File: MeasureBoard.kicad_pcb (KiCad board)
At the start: 2 copper layers, 60 x 80 mm, 129 parts, among them J1 Conn_01x06, J10 Conn_02x05_Odd_Even, J11 Conn_01x04, J12 Conn_01x06, J13 GS3, J14 USB_OTG, J15 Conn_01x02, J17 Conn_01x02, J18 Conn_01x03, J19 Conn_01x03, J2 Conn_01x04, J20 Conn_01x03, J21 Conn_01x03, J22 Conn_01x03, J23 Conn_01x03, J24 Conn_02x05_Odd_Even, J25 TEST_1P, J26 TEST_1P, J27 TEST_1P, J28 TEST_1P, J3 GS3, J4 GS2, J5 Conn_01x04, J6 Conn_01x03, J7 Conn_01x04, J8 BARREL_JACK, J9 CONN_01X02, SW1 DIP_SW_2P, SW2 SKRPACE010, SW3 SKRPACE010, SW4 SKRPACE010, U1 L7805, U2 AP1117-33, U3 STM32F103CBTx, U4 NC7SZ08, U5 SP3481CN, U6 NC7WZ241, U7 LTC2875-S8, U8 AM26LV32, Y1 Crystal

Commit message: gndのパスを修正
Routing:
- net GND: track 673.7 -> 663.9 mm, vias 119 -> 115
- net +5V: track 183.6 -> 188.9 mm
- net (no net): track 0.00 -> 1.64 mm, vias 0 -> 2
- net /CAN/CAN_H: track 13.1 -> 11.6 mm
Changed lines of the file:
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@@
-(kicad_pcb (version 4) (host pcbnew 4.0.7)
+(kicad_pcb (version 4) (host pcbnew 4.0.6)
   (general
     (links 311)
@@
     (thickness 1.6)
     (drawings 149)
-    (tracks 1607)
+    (tracks 1605)
     (zones 0)
     (modules 129)
@@
   (gr_line (start 54 150) (end 106 150) (layer Edge.Cuts) (width 0.15))
   (gr_line (start 50 74) (end 50 146) (layer Edge.Cuts) (width 0.15))
+  (segment (start 92 94.5) (end 90.5 94.5) (width 0.25) (layer F.Cu) (net 0))
+  (via (at 90.5 94.5) (size 0.6) (drill 0.4) (layers F.Cu B.Cu) (net 0))
+  (segment (start 92.1 94.6) (end 92 94.5) (width 0.25) (layer B.Cu) (net 0))
+  (via (at 92 94.5) (size 0.6) (drill 0.4) (layers F.Cu B.Cu) (net 0))
+  (segment (start 96 105.7) (end 95.35 105.7) (width 0.25) (layer F.Cu) (net 1))
+  (segment (start 95.35 105.7) (end 93.599999 107.450001) (width 0.25) (layer F.Cu) (net 1))
+  (segment (start 93.599999 107.450001) (end 93.599999 109.700001) (width 0.25) (layer F.Cu) (net 1))
+  (segment (start 93.599999 109.700001) (end 93.3 110) (width 0.25) (layer F.Cu) (net 1))
+  (segment (start 101 114.1) (end 99.93 114.1) (width 0.25) (layer F.Cu) (net 1))
+  (segment (start 99.93 114.1) (end 98.5 112.67) (width 0.25) (layer F.Cu) (net 1))
   (segment (start 93.6 113.3) (end 93.6 114.7) (width 0.25) (layer F.Cu) (net 1))
   (segment (start 93.6 114.7) (end 93.6 114.89) (width 0.25) (layer F.Cu) (net 1))
@@
   (segment (start 78.7 134) (end 78.9 133.8) (width 0.25) (layer B.Cu) (net 1))
   (via (at 78.9 133.8) (size 0.6) (drill 0.4) (layers F.Cu B.Cu) (net 1))
-  (segment (start 105.4 117.7) (end 103.7 117.7) (width 0.25) (layer F.Cu) (net 1))
-  (segment (start 103.7 117.7) (end 103.3 118.1) (width 0.25) (layer F.Cu) (net 1))
-  (via (at 103.3 118.1) (size 0.6) (drill 0.4) (layers F.Cu B.Cu) (net 1))
   (segment (start 101 114.1) (end 99.6 114.1) (width 0.25) (layer B.Cu) (net 1))
   (segment (start 99.6 114.1) (end 99 114.7) (width 0.25) (layer B.Cu) (net 1))
@@
   (via (at 93.8 89.8) (size 0.8) (drill 0.6) (layers F.Cu B.Cu) (net 1))
   (via (at 90.6 89.8) (size 0.8) (drill 0.6) (layers F.Cu B.Cu) (net 1))
-  (via (at 93.8 100) (size 0.8) (drill 0.6) (layers F.Cu B.Cu) (net 1))
   (segment (start 90.4 98.6) (end 90.4 100.6) (width 0.25) (layer B.Cu) (net 1))
   (via (at 90.4 100.6) (size 0.8) (drill 0.6) (layers F.Cu B.Cu) (net 1))
@@
   (segment (start 90.6 89.8) (end 93.8 89.8) (width 0.25) (layer F.Cu) (net 1))
   (segment (start 89.1 89.8) (end 90.6 89.8) (width 0.25) (layer B.Cu) (net 1))
-  (segment (start 92 94.5) (end 90.5 94.5) (width 0.25) (layer F.Cu) (net 1))
-  (via (at 90.5 94.5) (size 0.6) (drill 0.4) (layers F.Cu B.Cu) (net 1))
-  (segment (start 92.1 94.6) (end 92 94.5) (width 0.25) (layer B.Cu) (net 1))
-  (via (at 92 94.5) (size 0.6) (drill 0.4) (layers F.Cu B.Cu) (net 1))
   (segment (start 93.8 91.4) (end 93.8 93) (width 0.25) (layer B.Cu) (net 1))
   (segment (start 86.6 91.4) (end 93.8 91.4) (width 0.25) (layer F.Cu) (net 1))
@@
   (via (at 88.5 110.8) (size 0.6) (drill 0.4) (layers F.Cu B.Cu) (net 1))
   (via (at 93.3 110) (size 0.6) (drill 0.4) (layers F.Cu B.Cu) (net 1))
-  (segment (start 93.1 110.2) (end 93.3 110) (width 0.25) (layer F.Cu) (net 1))
   (segment (start 81.7 131.6) (end 81.7 133.5) (width 0.25) (layer F.Cu) (net 1))
   (via (at 81.6 133.6) (size 0.6) (drill 0.4) (layers F.Cu B.Cu) (net 1))
@@
   (segment (start 79.324264 134.4) (end 81.7 132.024264) (width 0.25) (layer F.Cu) (net 1))
   (segment (start 81.7 132.024264) (end 81.7 131.6) (width 0.25) (layer F.Cu) (net 1))
-  (segment (start 96 105.7) (end 96.65 105.7) (width 0.25) (layer F.Cu) (net 1))
-  (segment (start 96.65 105.7) (end 98.5 107.55) (width 0.25) (layer F.Cu) (net 1))
-  (segment (start 98.5 107.55) (end 98.5 112.245736) (width 0.25) (layer F.Cu) (net 1))
-  (segment (start 98.5 112.245736) (end 98.5 112.67) (width 0.25) (layer F.Cu) (net 1))
-  (segment (start 100.35 115.6) (end 102.725 115.6) (width 0.25) (layer F.Cu) (net 1))
-  (segment (start 102.725 115.6) (end 105.41 118.285) (width 0.25) (layer F.Cu) (net 1))
   (segment (start 105.41 118.285) (end 105.41 119.46) (width 0.25) (layer F.Cu) (net 1))
   (segment (start 101.25 115.6) (end 100.35 115.6) (width 0.25) (layer B.Cu) (net 1))
@@
   (segment (start 106.82 130.93) (end 108.25 129.5) (width 2) (layer B.Cu) (net 1))
   (segment (start 108.25 121) (end 106.71 119.46) (width 2) (layer B.Cu) (net 1))
+  (segment (start 98.3 106.2) (end 98.3 105.112614) (width 0.3) (layer F.Cu) (net 2))
+  (segment (start 94.3 111.4) (end 98.3 107.4) (width 0.3) (layer F.Cu) (net 2))
+  (segment (start 98.3 107.4) (end 98.3 106.2) (width 0.3) (layer F.Cu) (net 2))
+  (segment (start 103.2 120.5) (end 103.2 114.2) (width 0.8) (layer F.Cu) (net 2))
+  (segment (start 103.2 114.2) (end 102.5 113.5) (width 0.8) (layer F.Cu) (net 2))
+  (segment (start 102.5 113.5) (end 102.5 109.312614) (width 0.8) (layer F.Cu) (net 2))
+  (segment (start 102.5 109.312614) (end 98.3 105.112614) (width 0.8) (layer F.Cu) (net 2))
+  (segment (start 103.2 120.5) (end 103.2 120) (width 0.8) (layer F.Cu) (net 2))
+  (segment (start 103.2 124.7) (end 103.2 120.5) (width 0.8) (layer F.Cu) (net 2))
+  (segment (start 92 98.6) (end 93.337386 98.6) (width 0.8) (layer F.Cu) (net 2))
+  (segment (start 93.337386 98.6) (end 98.3 103.562614) (width 0.8) (layer F.Cu) (net 2))
+  (segment (start 98.3 103.562614) (end 98.3 105.112614) (width 0.8) (layer F.Cu) (net 2))
   (segment (start 63.1 96.7) (end 57.7 96.7) (width 1) (layer B.Cu) (net 2))
   (segment (start 57.7 96.7) (end 56.2 96.7) (width 1) (layer B.Cu) (net 2))
@@
   (segment (start 51.8 105.93) (end 51.8 104.5) (width 1) (layer B.Cu) (net 2))
   (via (at 51.8 104.5) (size 1) (drill 0.8) (layers F.Cu B.Cu) (net 2))
-  (segment (start 94.599999 111.699999) (end 94.599999 103.799999) (width 0.8) (layer F.Cu) (net 2))
-  (segment (start 92 101.2) (end 92 98.6) (width 0.8) (layer F.Cu) (net 2))
-  (segment (start 94.599999 103.799999) (end 92 101.2) (width 0.8) (layer F.Cu) (net 2))
   (segment (start 98.25 108.5) (end 98.25 110.95) (width 0.25) (layer B.Cu) (net 2))
   (segment (start 98.25 110.95) (end 97.8 111.4) (width 0.25) (layer B.Cu) (net 2))
@@
   (segment (start 92 96.5) (end 92 98.6) (width 1) (layer B.Cu) (net 2))
   (via (at 92 98.6) (size 1.2) (drill 0.8) (layers F.Cu B.Cu) (net 2))
-  (segment (start 94.6 117.4) (end 94.599999 111.699999) (width 0.8) (layer F.Cu) (net 2))
-  (segment (start 94.599999 111.699999) (end 94.3 111.4) (width 0.8) (layer F.Cu) (net 2))
-  (segment (start 95.2 118) (end 94.6 117.4) (width 0.8) (layer F.Cu) (net 2))
-  (segment (start 101.2 118) (end 95.2 118) (width 0.8) (layer F.Cu) (net 2))
-  (segment (start 103.2 120) (end 101.2 118) (width 0.8) (layer F.Cu) (net 2))
-  (segment (start 103.2 124.7) (end 103.2 120) (width 0.8) (layer F.Cu) (net 2))
   (segment (start 88.25 97.4) (end 88.75 96.9) (width 0.6) (layer B.Cu) (net 2))
   (segment (start 88.45 96.6) (end 88.75 96.9) (width 0.6) (layer B.Cu) (net 2))
@@
   (segment (start 102.3 136.435) (end 103.415 136.435) (width 0.4) (layer B.Cu) (net 34))
   (segment (start 103.415 136.435) (end 105.41 138.43) (width 0.4) (layer B.Cu) (net 34))
-  (segment (start 103.8 112.4) (end 102.905099 113.294901) (width 0.25) (layer F.Cu) (net 35))
-  (segment (start 102.905099 113.294901) (end 99.205099 113.294901) (width 0.25) (layer F.Cu) (net 35))
-  (segment (start 99.205099 113.294901) (end 96.46 116.04) (width 0.25) (layer F.Cu) (net 35))
+  (segment (start 102.4 112.67) (end 100.105146 112.67) (width 0.25) (layer B.Cu) (net 35))
+  (segment (start 100.105146 112.67) (end 96.575146 116.2) (width 0.25) (layer B.Cu) (net 35))
+  (segment (start 96.575146 116.2) (end 96.46 116.2) (width 0.25) (layer B.Cu) (net 35))
   (segment (start 96.46 116.04) (end 96.46 116.2) (width 0.25) (layer F.Cu) (net 35))
   (segment (start 103.8 112.4) (end 105.41 110.79) (width 0.25) (layer F.Cu) (net 35))

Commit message: update
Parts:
- moved J3 3.20 mm to (51.8, 104.0)
- moved R6 0.71 mm to (60.1, 106.1), turned to 90 degrees
- moved R7 0.41 mm to (61.6, 106.1), turned to 90 degrees
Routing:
- net GND: track 663.9 -> 738.7 mm, vias 115 -> 137
- net +3V3: track 285.7 -> 289.7 mm, vias 17 -> 16
- net Net-(J2-Pad1): track 5.36 -> 2.91 mm
- net /MCU/I2C1_SCL: track 29.2 -> 31.1 mm, vias 0 -> 1
- net /MCU/I2C1_SDA: track 29.5 -> 31.3 mm, vias 0 -> 1
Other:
- board text added: "L433"

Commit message: 一回区切りついた
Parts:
- moved D9 42.0 mm to (54.7, 98.7), turned to 0 degrees
- moved R16 39.8 mm to (59.0, 98.4), turned to 90 degrees
- moved R21 25.4 mm to (70.4, 114.1), turned to 90 degrees
- moved R20 23.5 mm to (68.9, 114.1), turned to 270 degrees
- moved R17 14.4 mm to (63.9, 108.7), turned to 180 degrees
- moved D10 10.9 mm to (67.0, 108.7), turned to 180 degrees
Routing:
- net GND: track 738.7 -> 1039.1 mm, vias 137 -> 232
- net Net-(J14-Pad2): track 3.44 -> 31.8 mm
- net /USB/D-: track 37.7 -> 9.85 mm
- net Net-(J14-Pad3): track 3.47 -> 30.9 mm
- net /USB/D+: track 35.6 -> 9.62 mm
- net +5V: track 188.9 -> 181.5 mm
- net +3V3: track 289.7 -> 285.9 mm
- net Net-(D9-Pad2): track 1.77 -> 3.69 mm

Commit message: udpate
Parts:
- moved D5 4.80 mm to (64.2, 94.7), turned to 90 degrees
- moved C1 3.36 mm to (71.1, 95.4)
- moved J1 3.00 mm to (67.2, 93.4)
- moved J11 3.00 mm to (69.8, 90.8)
- moved J27 3.00 mm to (54.0, 77.0)
- moved J28 3.00 mm to (106.0, 77.0)
- moved J4 3.00 mm to (80.8, 90.6)
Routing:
- net GND: track 1039.1 -> 931.4 mm, vias 232 -> 207
- net (no net): track 1.64 -> 5.84 mm, vias 2 -> 4
- net +5V: track 181.5 -> 185.5 mm
- net /MCU/USART1_RX: track 46.8 -> 44.9 mm
- net +3V3: track 285.9 -> 284.5 mm
- net /MCU/USART1_TX: track 47.9 -> 46.6 mm
- net Net-(D5-Pad2): track 8.15 -> 6.94 mm
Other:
- board size 60 x 80 mm -> 60 x 77 mm

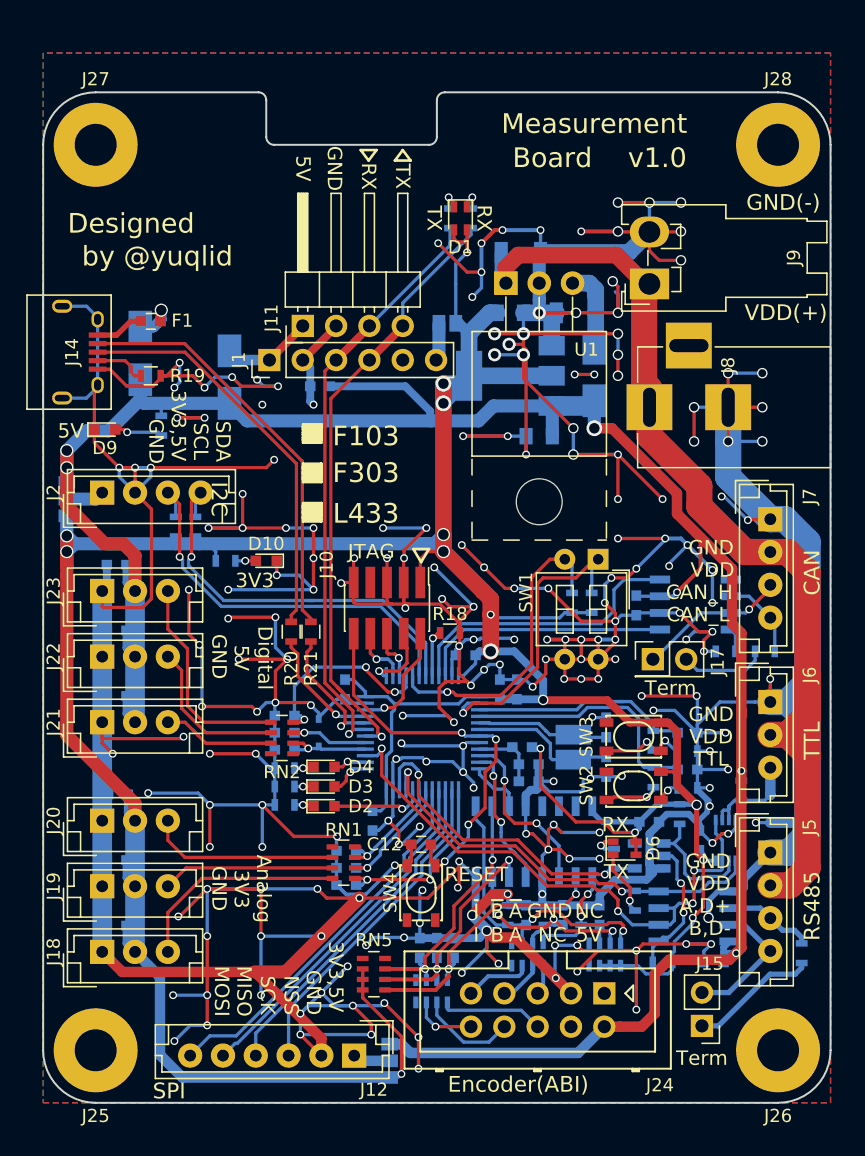
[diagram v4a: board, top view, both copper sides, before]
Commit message: コモンモードフィルタつけた
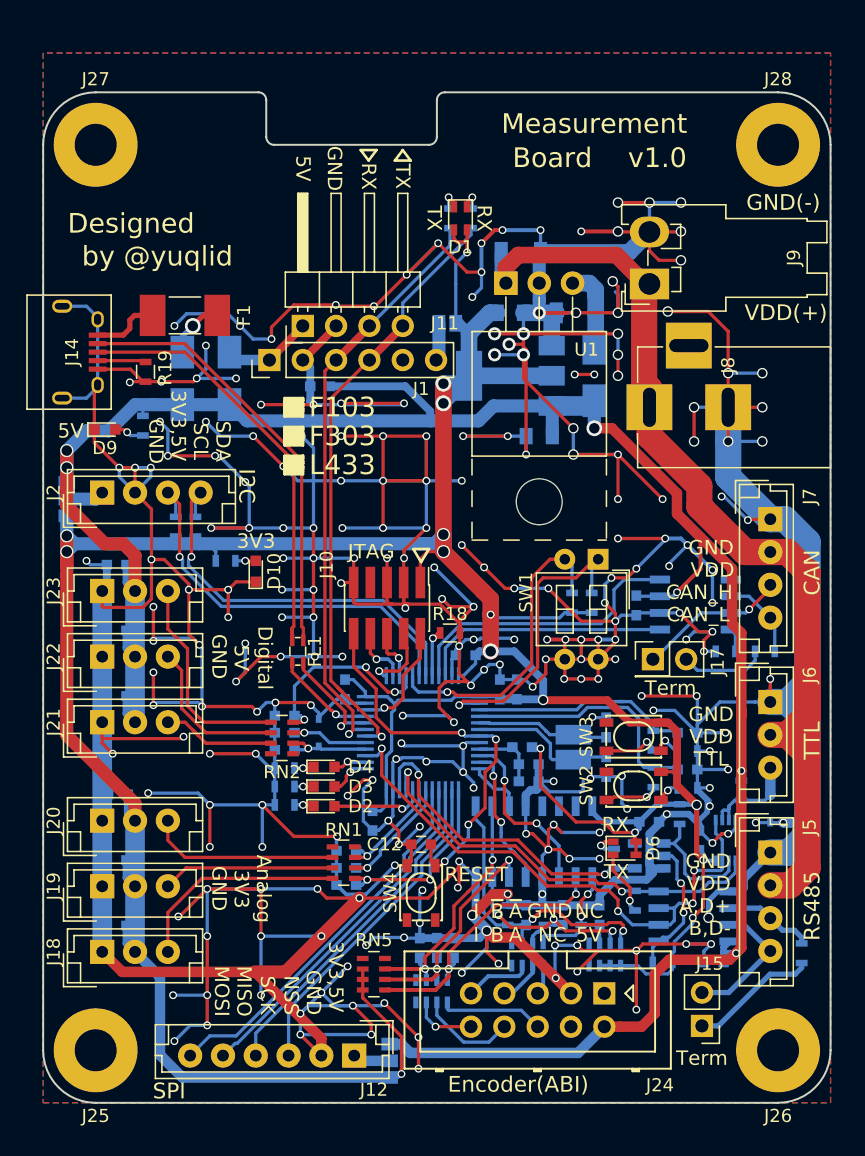
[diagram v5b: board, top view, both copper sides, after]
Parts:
- removed R20, R21: 24, Resistors_SMD:R_0603
- added FL1: EMI_Filter_CommonMode, Inductors_SMD:L_Murata_DLW21HN900SQ2#, F.Cu at (69.4, 115.6)
- F1: footprint Capacitors_SMD:C_0603 -> Fuse_Holders_and_Fuses:Fuse_0679H
- moved D11 3.72 mm to (60.6, 94.8)
- moved F1 2.64 mm to (60.8, 90.0)
- moved R16 1.40 mm to (57.6, 98.4)
- moved D10 1.13 mm to (66.2, 109.5), turned to 90 degrees
- moved R19 0.50 mm to (57.8, 94.3), turned to 270 degrees
- moved D5 0.10 mm to (64.2, 94.8)
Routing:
- net GND: track 931.4 -> 1075.0 mm, vias 207 -> 245
- net (no net): track 5.84 -> 1.64 mm, vias 4 -> 2
- net +5V: track 185.5 -> 183.2 mm
- net /USB/D+: track 9.62 -> 7.68 mm
- net Net-(FL1-Pad3): track 30.9 -> 32.6 mm
- net /USB/D-: track 9.85 -> 8.24 mm
- net Net-(FL1-Pad1): track 31.8 -> 33.3 mm
- net Net-(F1-Pad2): track 3.73 -> 5.19 mm
- net Net-(D9-Pad2): track 3.69 -> 2.29 mm
- net Net-(D11-Pad2): track 3.84 -> 4.52 mm

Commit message: 再アノテーション，電解コンデンサ追加
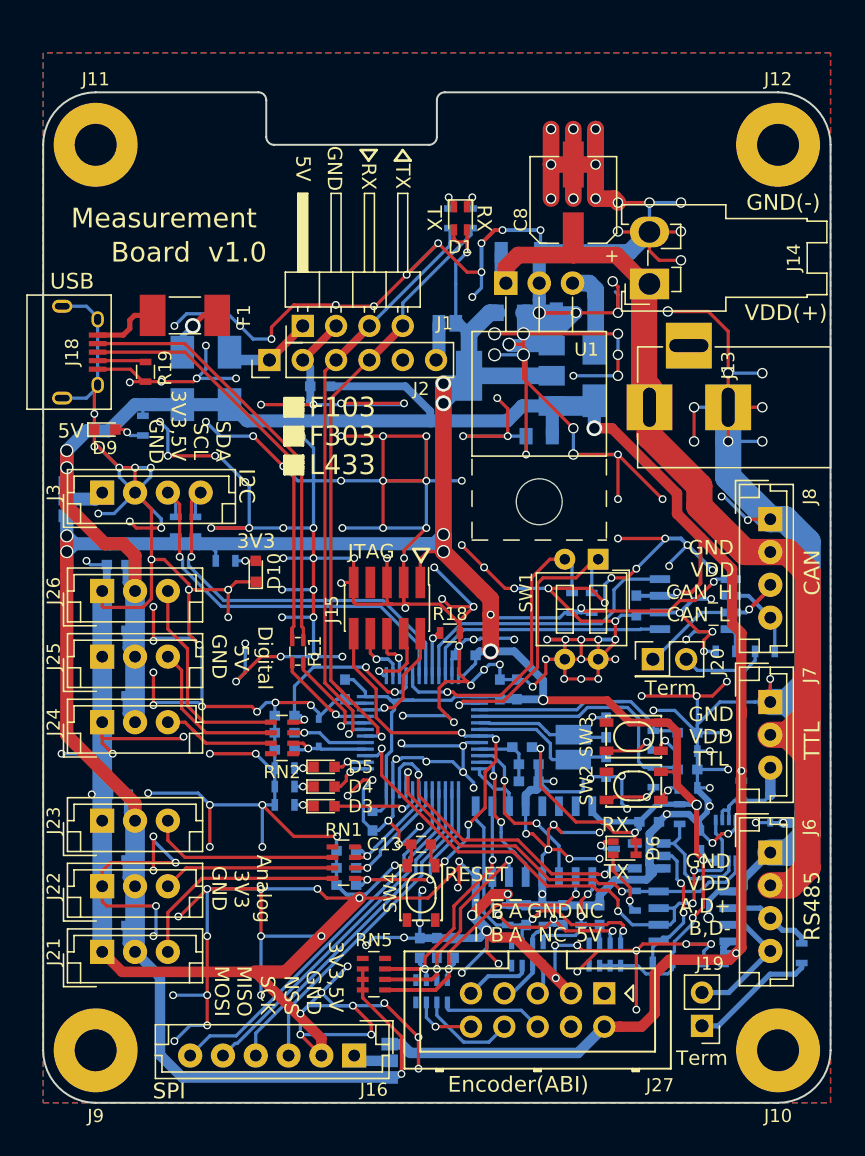
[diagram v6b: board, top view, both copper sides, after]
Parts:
- added C8: CP, Capacitors_SMD:CP_Elec_6.3x7.7, F.Cu at (90.4, 81.2)
- RN1, RN5: value R_Pack04 -> 10k_4
- RN2, RN3, RN4: value R_Pack04 -> 150_4
- RN6: value R_Pack04 -> 20k_4
- U7: value LTC2875-S8 -> MCP2562-E-SN
- renumbered C9 to C10, C10 to C11, C11 to C12, C12 to C13, C13 to C14, C14 to C15, C15 to C16, C16 to C17, C17 to C18, C18 to C19, C19 to C20, C20 to C21, C21 to C22, C22 to C23, C23 to C24, C24 to C25, C25 to C26, C26 to C27, C27 to C28, C28 to C29, C29 to C30, C30 to C31, C31 to C32, C32 to C33, C33 to C34, C34 to C35, C35 to C36, C36 to C37, C37 to C38, C38 to C39, C39 to C40, C8 to C9, D5 to D2, D2 to D3, D3 to D4, D4 to D5, J11 to J1, J26 to J10, J27 to J11, J28 to J12, J8 to J13, J9 to J14, J10 to J15, J12 to J16, J13 to J17, J14 to J18, J15 to J19, J1 to J2, J17 to J20, J18 to J21, J19 to J22, J20 to J23, J21 to J24, J22 to J25, J23 to J26, J24 to J27, J2 to J3, J3 to J4, J4 to J5, J5 to J6, J6 to J7, J7 to J8, J25 to J9, R22 to R20, R23 to R21, R24 to R22, R25 to R23, R30 to R24, R26 to R25, R27 to R26, R28 to R27, R29 to R28
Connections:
- U7 pad 5: Net-(U7-Pad5) -> +3V3
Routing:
- net GND: track 1075.0 -> 1161.2 mm, vias 245 -> 267
- net +3V3: track 284.5 -> 299.2 mm, vias 16 -> 18
- net (no net): track 1.64 -> 0.00 mm, vias 2 -> 0
- net +12V: track 79.7 -> 81.2 mm
- net +5V: track 183.2 -> 183.9 mm
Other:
- board text added: "USB"
